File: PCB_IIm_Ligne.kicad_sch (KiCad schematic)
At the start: 42 parts, among them J1 Screw_Terminal_01x08, J2 Screw_Terminal_01x08, J3 Screw_Terminal_01x08, K1 G2RK-2 DC12, K2 Relay_DPDT_Latching_2coil, Q1 MPSA56, Q2 2N2222A, Q3 2N2222A, Q4 2N2222A, Q6 IRF40B207, U1 TLC555xP

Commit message: BOM update, new relay + new P side mosfet + Aliexpress links and price
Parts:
- added J4, J5, J6: Screw_Terminal_01x06, TerminalBlock_Phoenix:TerminalBlock_Phoenix_MPT-0,5-6-2.54_1x06_P2.54mm_Horizontal, symbol Connector:Screw_Terminal_01x06
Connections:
- net +12V: now also J4.1 (Pin_1), J5.1 (Pin_1)
- net GND: now also J4.6 (Pin_6), J5.6 (Pin_6), J6.6 (Pin_6)
- new net + Traction: J4.2 (Pin_2), J5.2 (Pin_2)
- new net Etat Sens de A: J4.4 (Pin_4)
- new net Etat Sens de B: J5.4 (Pin_4)
- new net Impulsion Sens de A: J4.3 (Pin_3)
- new net Impulsion Sens de B: J5.3 (Pin_3)
- new net LED Alim en service: J6.1 (Pin_1)
- new net LED Sens A: J6.3 (Pin_3)
- new net LED Sens B: J6.4 (Pin_4)
- new net LED Traction en service: J6.2 (Pin_2)

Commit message: recomit
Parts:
- removed J4, J5, J6: Screw_Terminal_01x06, TerminalBlock_Phoenix:TerminalBlock_Phoenix_MPT-0,5-6-2.54_1x06_P2.54mm_Horizontal, symbol Connector:Screw_Terminal_01x06
- added D5: D, Diode_THT:D_DO-15_P10.16mm_Horizontal, symbol Device:D
- added J4: Screw_Terminal_01x08, TerminalBlock_Phoenix:TerminalBlock_Phoenix_MPT-0,5-8-2.54_1x08_P2.54mm_Horizontal, symbol Connector:Screw_Terminal_01x08
- added R3: 1R 2W, symbol Device:R
- R4: value 220 -> 1K
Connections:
- net +20V: now also D5.1 (K)
- net Traction_P: now also D5.2 (A)

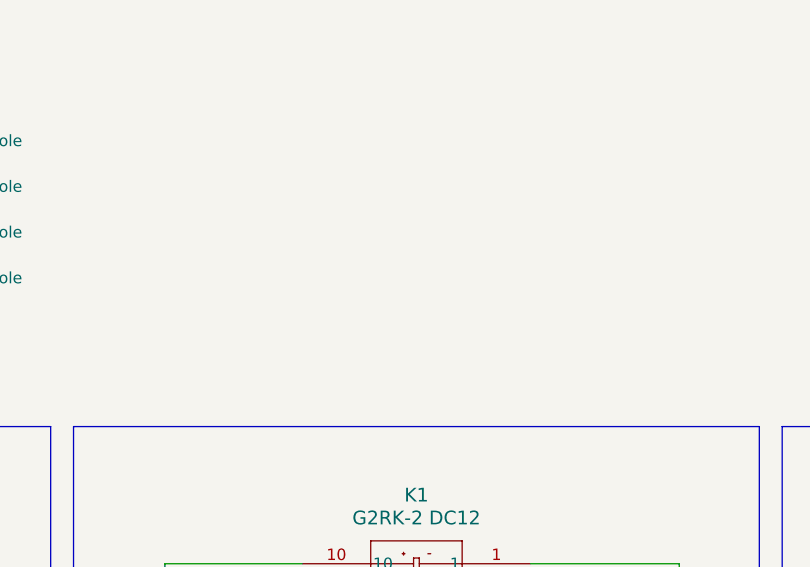
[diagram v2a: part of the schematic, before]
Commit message: Finder relay Lib
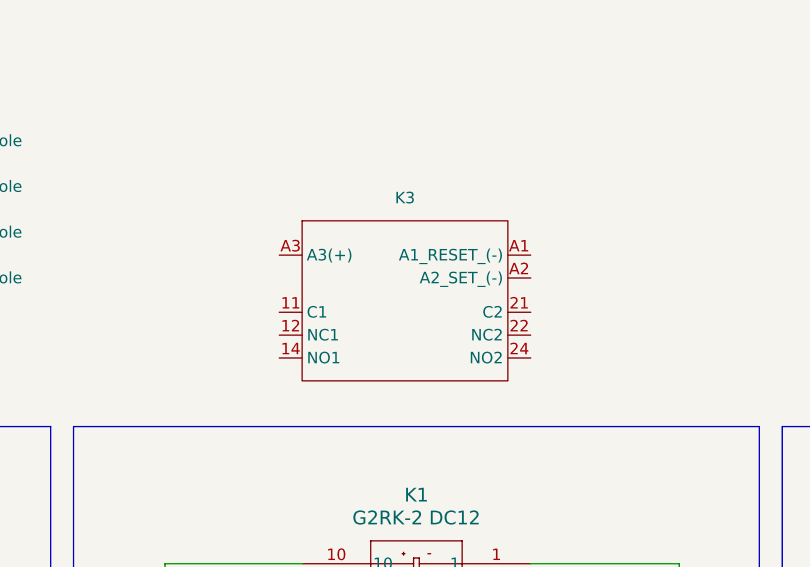
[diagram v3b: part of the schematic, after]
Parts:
- added K3: (no value), Library_IIm:Finder_41.52.6.012.4016, symbol Finder_41526:Finder_41.52.6.012.4016
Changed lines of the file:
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@@
+	)
+	(symbol
+		(lib_id "Finder_41526:Finder_41.52.6.012.4016")
+		(at 412.75 -10.16 0)
+		(unit 1)
+		(body_style 1)
+		(exclude_from_sim no)
+		(in_bom yes)
+		(on_board yes)
+		(in_pos_files yes)
+		(dnp no)
+		(fields_autoplaced yes)
+		(property "Reference" "K3"
+			(at 412.75 -10.16 0)
+			(show_name no)
+			(do_not_autoplace no)
+			(effects
+				(font
+					(size 1.27 1.27)
+				)
+			)
+		)
+		(property "Value" ""
+			(at 412.75 -10.16 0)
+			(show_name no)
+			(do_not_autoplace no)
+			(effects
+				(font
+					(size 1.27 1.27)
+				)
+			)
+		)
+		(property "Footprint" "Library_IIm:Finder_41.52.6.012.4016"
+			(at 412.75 -10.16 0)
+			(hide yes)
+			(show_name no)
+			(do_not_autoplace no)
+			(effects
+				(font
+					(size 1.27 1.27)
+				)
+			)
+		)
+		(property "Datasheet" ""
+			(at 412.75 -10.16 0)
+			(hide yes)
+			(show_name no)
+			(do_not_autoplace no)
+			(effects
+				(font
+					(size 1.27 1.27)
+				)
+			)
+		)
+		(property "Description" ""
+			(at 412.75 -10.16 0)
+			(hide yes)
+			(show_name no)
+			(do_not_autoplace no)
+			(effects
+				(font
+					(size 1.27 1.27)
+				)
+			)
+		)
+		(pin "A1"
+		)
+		(pin "21"
+		)
+		(pin "14"
+		)
+		(pin "11"
+		)
+		(pin "12"
+		)
+		(pin "24"
+		)
+		(pin "A3"
+		)
+		(pin "A2"
+		)
+		(pin "22"
+		)
+		(instances
+			(project "PCB_IIm_Ligne"
+				(path "/d84f5e4c-0932-47c3-8773-68a666a48e8b"
+					(reference "K3")
+					(unit 1)
+				)
+			)
+		)
 	)
 	(symbol

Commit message: Modif Schematic + Layout
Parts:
- removed JP3, JP4: SolderJumper_2_Bridged, symbol Jumper:SolderJumper_2_Bridged
- removed K1: G2RK-2 DC12, RELAY_G2RK-2_OMR, symbol Omron_G2RK-2 12DC:G2RK-2_DC12
- renumbered K3 to K1
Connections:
- net +20V: now also J3.7 (Pin_7), J3.8 (Pin_8); no longer J3.5 (Pin_5), J3.6 (Pin_6)
- net GND: now also K1.14 (NO1), K1.22 (NC2); no longer D1.2 (A), D2.2 (A)
- net RAIL_1: now also J3.6 (Pin_6), K1.21 (C2); no longer J3.8 (Pin_8)
- net RAIL_2: now also J3.5 (Pin_5), K1.11 (C1); no longer J3.7 (Pin_7)
- net RelaiBistableSensA: no longer D2.1 (K), K2.1
- net RelaiBistableSensA_N: now also D1.2 (A), K1.A1 (A1_RESET_(-))
- net RelaiBistableSensB: no longer D1.1 (K), K2.2
- net RelaiBistableSensB_N: now also D2.2 (A), K1.A2 (A2_SET_(-))
- net Traction_P: now also K1.12 (NC1), K1.24 (NO2)
- net VCC: now also D1.1 (K), D2.1 (K), K1.A3 (A3(+)), K2.1, K2.2
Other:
- note added: "Relai BiStable Puissance"
- note removed: "Relai BiStable Puissance - Omron G2RK-2 12 DC"
- moved on the sheet: D1, D2, K1, K2

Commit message: kicad modif
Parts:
- added D6: D_Zener, Diode_THT:D_DO-15_P10.16mm_Horizontal, symbol Device:D_Zener
- R3: footprint (none) -> Resistor_THT:R_Axial_DIN0411_L9.9mm_D3.6mm_P12.70mm_Horizontal
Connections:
- net +20V: now also R3.1, D6.1 (K)
- net GND: now also D6.2 (A)
- net ResistanceShunt: now reaches J4.1 (Pin_1)
- net ResistanceShunt: now also R3.2
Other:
- moved on the sheet: J4

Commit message: Kicad Schematic organisation
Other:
- note added: "Connecteur Puissance 5.08mm"
- note removed: "Connecteur Alimentation"
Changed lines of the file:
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@@
 		)
 	)
-	(text "Connecteur Alimentation\n\n"
+	(text "Connecteur Puissance 5.08mm\n\n\n"
 		(exclude_from_sim no)
 		(at 312.166 144.272 0)

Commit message: Reorganisation Etiquette et schematic
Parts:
- removed JP1: SolderJumper_3_Open, Jumper:SolderJumper-3_P1.3mm_Open_RoundedPad1.0x1.5mm, symbol Jumper:SolderJumper_3_Open
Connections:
- net CommandetTraction is gone; now on net CommandeTraction: R12.1 (+), U1.3 (Q)
- net +12V: no longer J3.2 (Pin_2)
- net +20V: now also C1.1, J3.5 (Pin_5); no longer J3.7 (Pin_7), J3.8 (Pin_8)
- net ArduinoRelaiBistableSensA: now also J4.4 (Pin_4); no longer J2.4 (Pin_4)
- net ArduinoRelaiBistableSensB: now also J4.3 (Pin_3); no longer J2.3 (Pin_3)
- net GND: now also J3.2 (Pin_2); no longer J3.3 (Pin_3), J3.4 (Pin_4)
- net RAIL_1: now also J3.4 (Pin_4); no longer J3.6 (Pin_6)
- net RAIL_2: now also J3.3 (Pin_3); no longer J3.5 (Pin_5)
- net Traction_P: no longer C1.1
- net CommandeTraction: now reaches J4.2 (Pin_2)
- net OUT_ARD: no longer names the net of J2.2 (Pin_2)
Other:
- note added: "Mosfet traction"
- note added: "PWM Generator - 1KHz"
- note removed: "Commande Traction"
- note removed: "Selection Pot/Arduino (Option Justin)"
- moved on the sheet: C1, C2, C3, C4, C5, D3, D4, D5, Q4, Q6, R1, R12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
